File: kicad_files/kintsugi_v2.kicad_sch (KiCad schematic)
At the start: 162 parts, among them J1 Conn_01x04, J2 Conn_01x04, J3 AudioJack4, J4 AudioJack4, SW1 RotaryEncoder_Switch, SW2 SW_Push, U1 ProMicro, U2 MCP23017_SP

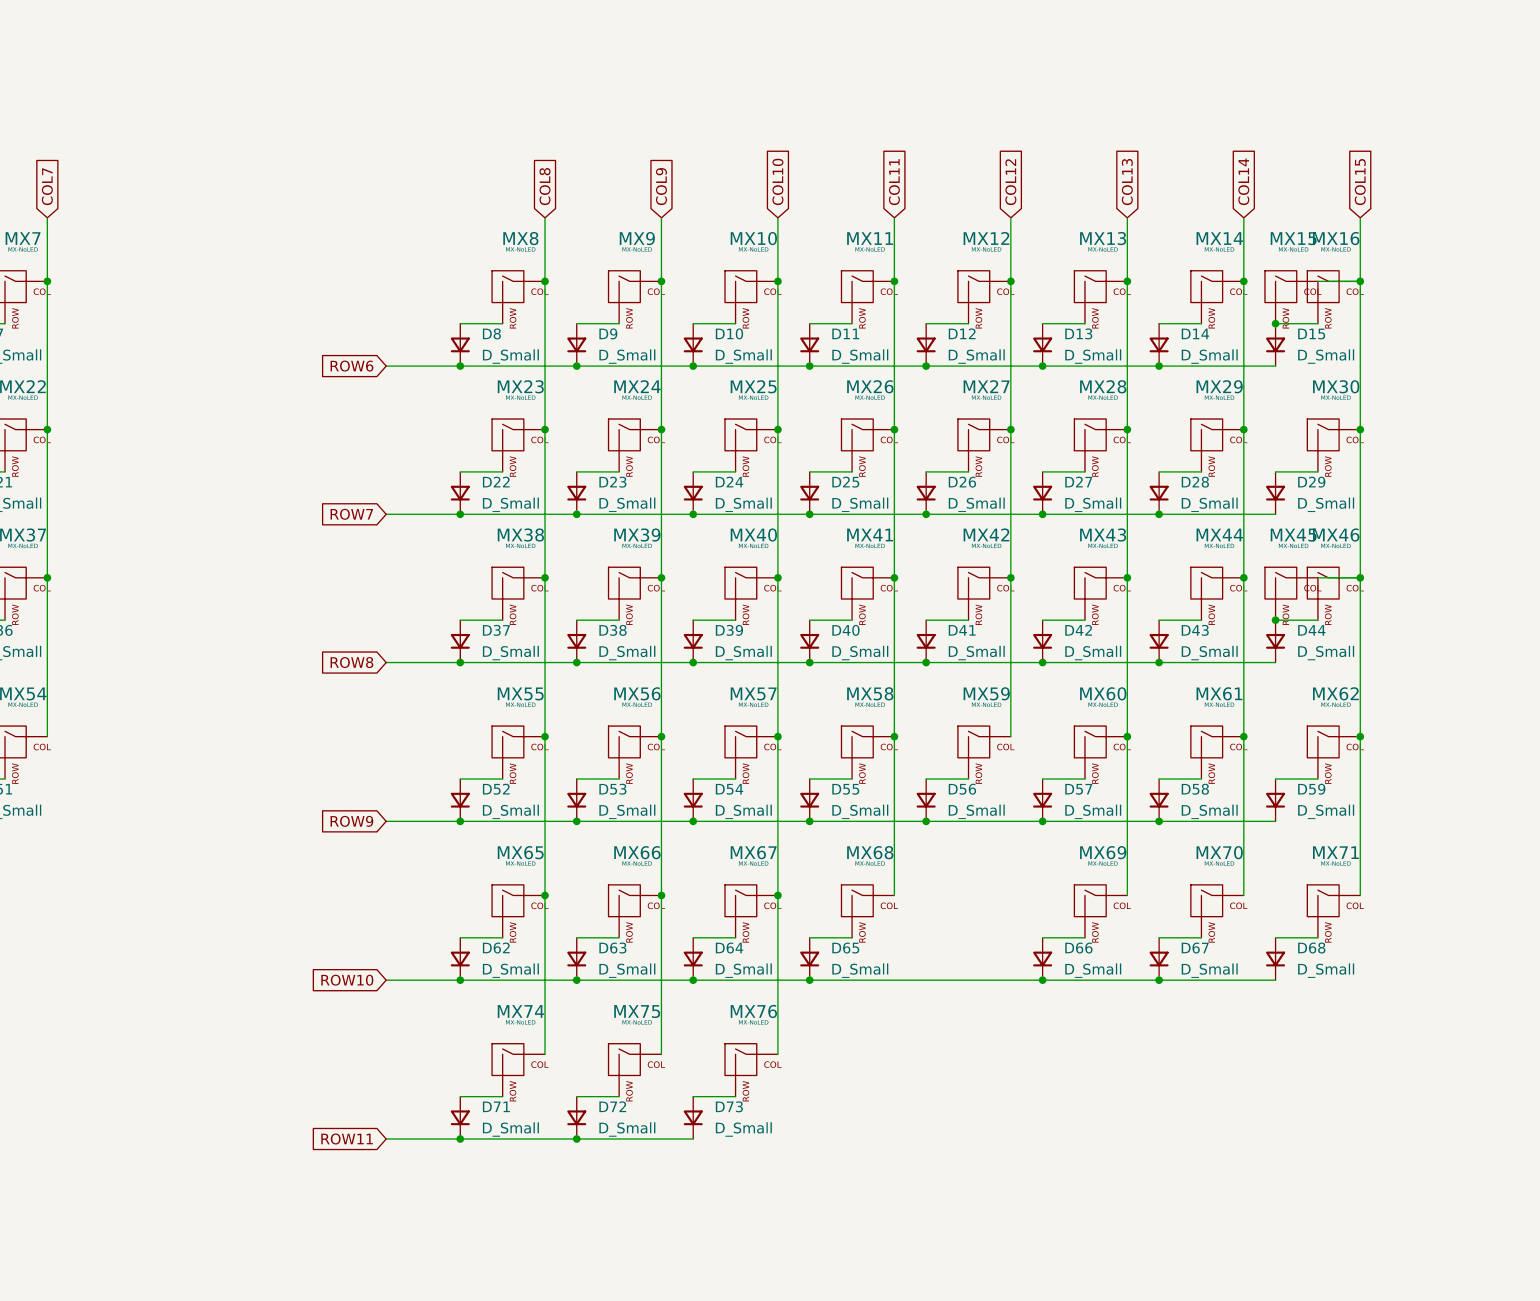
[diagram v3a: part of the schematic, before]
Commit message: Routed sockets pads to diodes. Pending review.
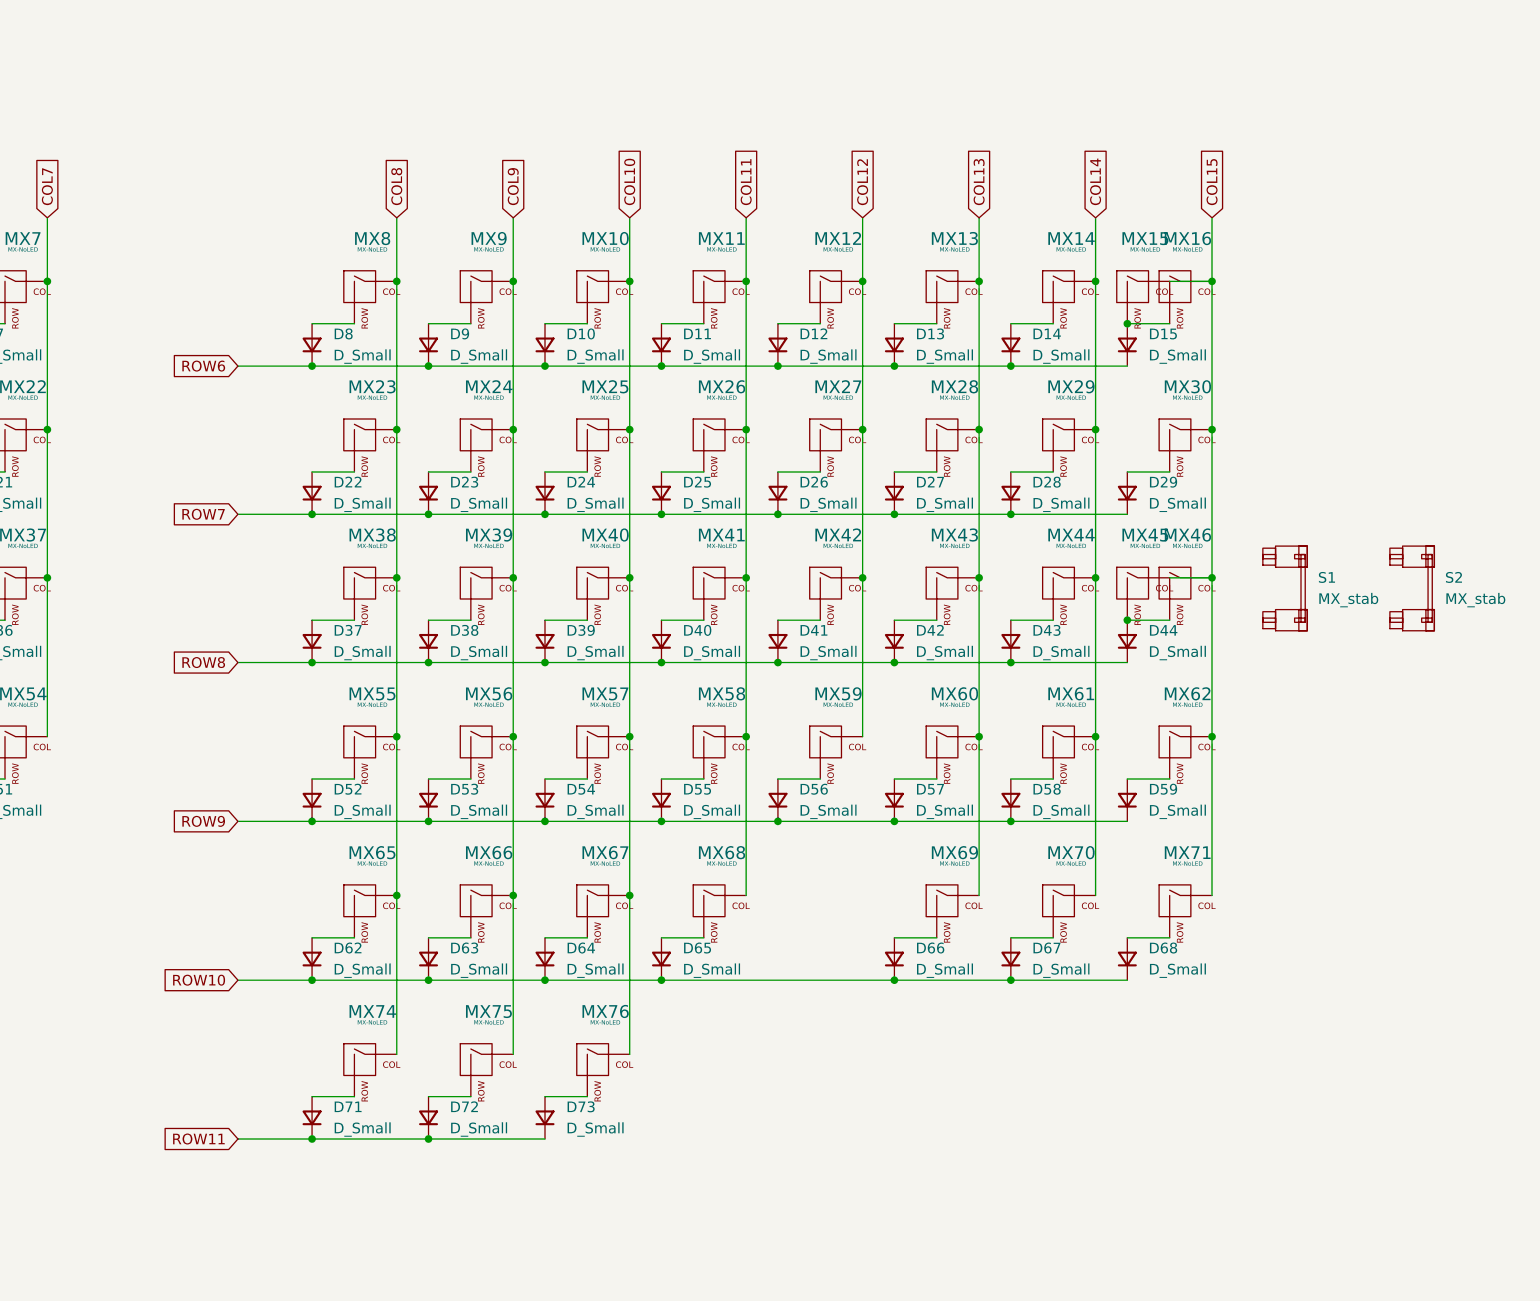
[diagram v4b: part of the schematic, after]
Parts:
- added S1: MX_stab, marbastlib-mx:STAB_MX_ISO_FLIPPED, symbol marbastlib-mx:MX_stab
- added S2: MX_stab, marbastlib-mx:STAB_MX_2.25u, symbol marbastlib-mx:MX_stab
- MX30: footprint acheron_MXH_metalrings:MX150H -> acheron_MXH_metalrings:MX100H
- MX45: footprint acheron_MXH_metalrings:MX225H -> acheron_MXH_metalrings:MX100H
- MX46: footprint acheron_MXH_metalrings:MX_ISOEnterH -> acheron_MXH_metalrings:MX100H
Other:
- moved on the sheet: D10, D11, D12, D13, D14, D15, D22, D23, D24, D25, D26, D27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

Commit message: Routed rows of the right side (down view) to the MCU.
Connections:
- net COL6: now also U1.13 (10/PB6); no longer U1.1 (TX0/PD3)
- net COL7: now also U1.14 (16/PB2); no longer U1.2 (RX1/PD2)
- net ENCA: now also U1.12 (9/PB5); no longer U1.11 (8/PB4)
- net ENCB: now also U1.11 (8/PB4); no longer U1.12 (9/PB5)
- net ROW0: now also U1.1 (TX0/PD3); no longer U1.7 (4/PD4)
- net ROW1: now also U1.2 (RX1/PD2); no longer U1.8 (5/PC6)
- net ROW2: now also U1.7 (4/PD4); no longer U1.9 (6/PD7)
- net ROW3: now also U1.8 (5/PC6); no longer U1.10 (7/PE6)
- net ROW4: now also U1.10 (7/PE6); no longer U1.13 (10/PB6)
- net ROW5: now also U1.9 (6/PD7); no longer U1.14 (16/PB2)

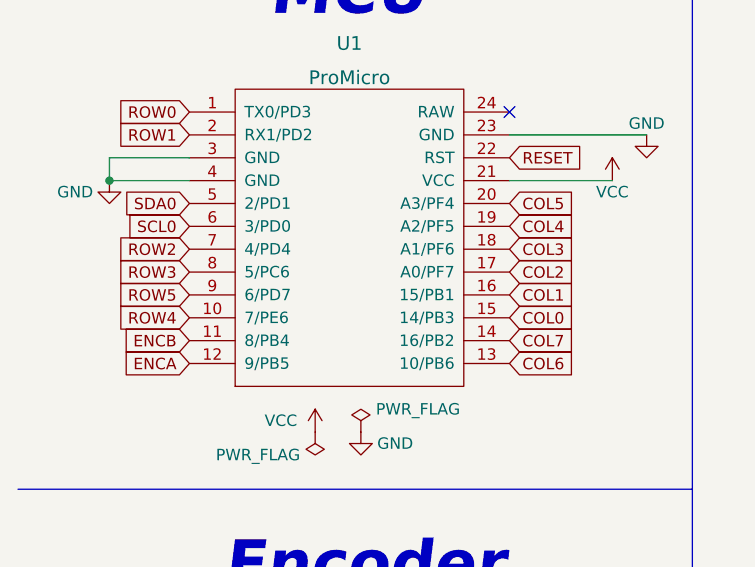
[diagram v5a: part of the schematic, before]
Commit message: Filleted edge cuts.
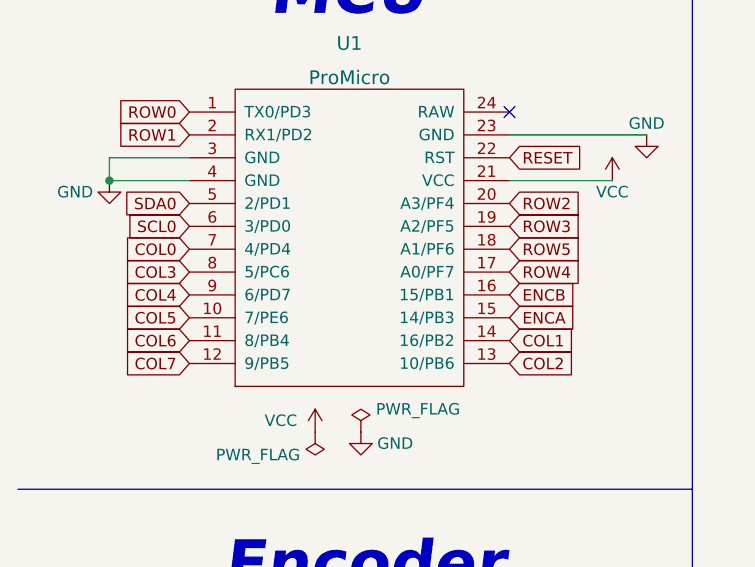
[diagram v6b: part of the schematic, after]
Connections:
- net COL0: now also U1.7 (4/PD4); no longer U1.15 (14/PB3)
- net COL1: now also U1.14 (16/PB2); no longer U1.16 (15/PB1)
- net COL2: now also U1.13 (10/PB6); no longer U1.17 (A0/PF7)
- net COL3: now also U1.8 (5/PC6); no longer U1.18 (A1/PF6)
- net COL4: now also U1.9 (6/PD7); no longer U1.19 (A2/PF5)
- net COL5: now also U1.10 (7/PE6); no longer U1.20 (A3/PF4)
- net COL6: now also U1.11 (8/PB4); no longer U1.13 (10/PB6)
- net COL7: now also U1.12 (9/PB5); no longer U1.14 (16/PB2)
- net ENCA: now also U1.15 (14/PB3); no longer U1.12 (9/PB5)
- net ENCB: now also U1.16 (15/PB1); no longer U1.11 (8/PB4)
- net ROW2: now also U1.20 (A3/PF4); no longer U1.7 (4/PD4)
- net ROW3: now also U1.19 (A2/PF5); no longer U1.8 (5/PC6)
- net ROW4: now also U1.17 (A0/PF7); no longer U1.10 (7/PE6)
- net ROW5: now also U1.18 (A1/PF6); no longer U1.9 (6/PD7)

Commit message: Added mousebites, re-arranged PCB and ground-filled half of the keyboard.
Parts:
- added H1, H10, H11, H12, H2, H3, H4, H5, H6, H7, H8, H9: MountingHole, Keebio-Parts:breakaway-mousebites, symbol Mechanical:MountingHole

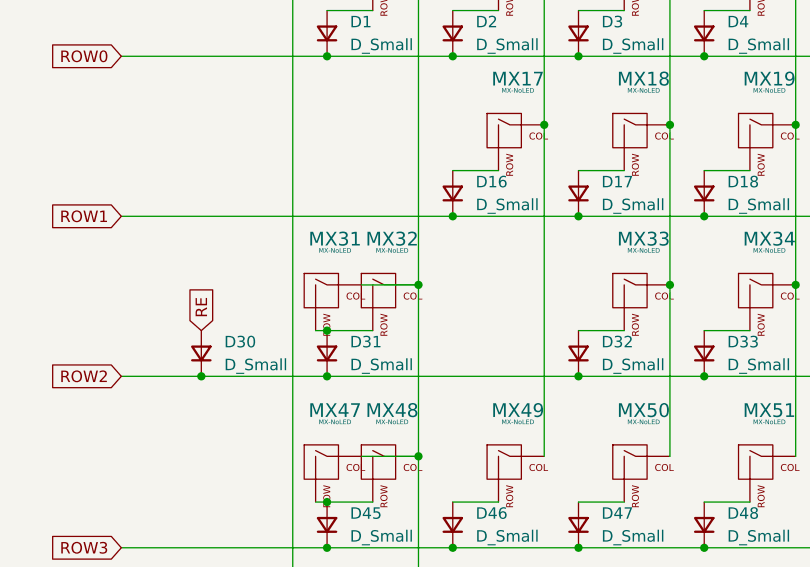
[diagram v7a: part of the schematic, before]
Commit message: Fixed some errors on the layout of the switch matrix.
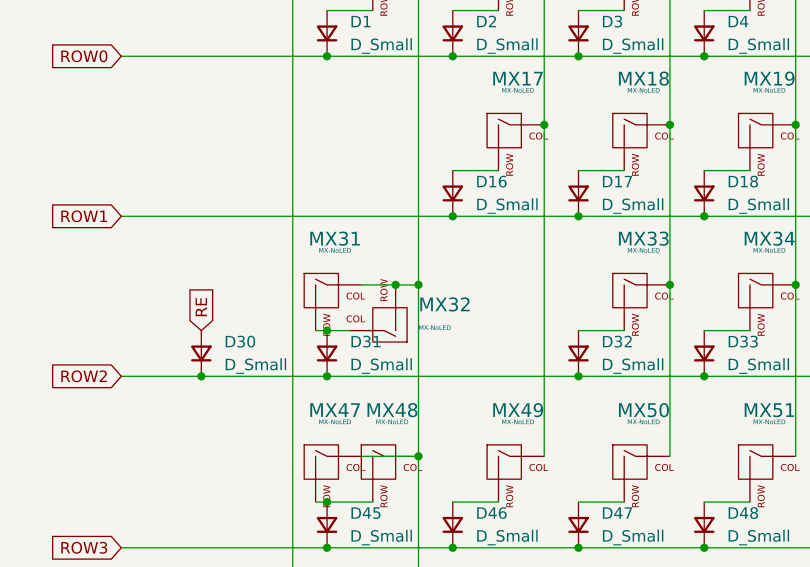
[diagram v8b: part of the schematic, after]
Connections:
- net COL1: now also MX32.2 (ROW); no longer MX32.1 (COL)
- net at D31.2 (A), MX31.2 (ROW): now also MX32.1 (COL); no longer MX32.2 (ROW)
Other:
- moved on the sheet: MX32
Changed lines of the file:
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@@
   (junction (at 149.86 72.39) (diameter 0) (color 0 0 0 0)
   )
+  (junction (at 135.89 85.09) (diameter 0) (color 0 0 0 0)
+  )
   (junction (at 275.59 54.61) (diameter 0) (color 0 0 0 0)
   )
@@
   (junction (at 285.75 80.01) (diameter 0) (color 0 0 0 0)
   )
-  (junction (at 135.89 85.09) (diameter 0) (color 0 0 0 0)
-  )
   (junction (at 299.72 80.01) (diameter 0) (color 0 0 0 0)
   )
@@
   (junction (at 215.9 44.45) (diameter 0) (color 0 0 0 0)
   )
+  (junction (at 143.51 80.01) (diameter 0) (color 0 0 0 0)
+  )
   (junction (at 299.72 99.06) (diameter 0) (color 0 0 0 0)
   )
@@
     (stroke (width 0) (type default) (color 0 0 0 0))
   )
+  (wire (pts (xy 143.51 80.01) (xy 146.05 80.01))
+    (stroke (width 0) (type default) (color 0 0 0 0))
+  )
   (wire (pts (xy 205.74 85.09) (xy 210.82 85.09))
     (stroke (width 0) (type default) (color 0 0 0 0))
@@
     (stroke (width 0) (type default) (color 0 0 0 0))
   )
+  (wire (pts (xy 139.7 80.01) (xy 143.51 80.01))
+    (stroke (width 0) (type default) (color 0 0 0 0))
+  )
   (polyline (pts (xy 87.63 115.57) (xy 87.63 77.47))
     (stroke (width 0) (type default) (color 0 0 0 0))
@@
     (stroke (width 0) (type default) (color 0 0 0 0))
   )
-  (wire (pts (xy 135.89 85.09) (xy 140.97 85.09))
-    (stroke (width 0) (type default) (color 0 0 0 0))
-  )
   (wire (pts (xy 205.74 67.31) (xy 210.82 67.31))
     (stroke (width 0) (type default) (color 0 0 0 0))
@@
     (stroke (width 0) (type default) (color 0 0 0 0))
   )
+  (wire (pts (xy 135.89 85.09) (xy 138.43 85.09))
+    (stroke (width 0) (type default) (color 0 0 0 0))
+  )
   (wire (pts (xy 299.72 62.23) (xy 299.72 80.01))
     (stroke (width 0) (type default) (color 0 0 0 0))
@@
     (stroke (width 0) (type default) (color 0 0 0 0))
   )
-  (wire (pts (xy 139.7 80.01) (xy 146.05 80.01))
-    (stroke (width 0) (type default) (color 0 0 0 0))
-  )
   (wire (pts (xy 163.83 54.61) (xy 177.8 54.61))
     (stroke (width 0) (type default) (color 0 0 0 0))
@@
     (pin "2")
   )
-  (symbol (lib_id "MX_Alps_Hybrid:MX-NoLED") (at 142.24 81.28 0) (unit 1)
+  (symbol (lib_id "MX_Alps_Hybrid:MX-NoLED") (at 142.24 83.82 180) (unit 1)
     (in_bom yes) (on_board yes) (fields_autoplaced)
-    (property "Reference" "MX32" (id 0) (at 143.1256 74.93 0)
-      (effects (font (size 1.524 1.524)))
+    (property "Reference" "MX32" (id 0) (at 146.05 82.2393 0)
+      (effects (font (size 1.524 1.524)) (justify right))
     )
-    (property "Value" "MX-NoLED" (id 1) (at 143.1256 76.2 0)
-      (effects (font (size 0.508 0.508)))
+    (property "Value" "MX-NoLED" (id 1) (at 146.05 84.7792 0)
+      (effects (font (size 0.508 0.508)) (justify right))
     )
-    (property "Footprint" "acheron_MXH_metalrings:MX175H" (id 2) (at 126.365 81.915 0)
+    (property "Footprint" "acheron_MXH_metalrings:MX175H" (id 2) (at 158.115 83.185 0)
       (effects (font (size 1.524 1.524)) hide)
     )
-    (property "Datasheet" "" (id 3) (at 126.365 81.915 0)
+    (property "Datasheet" "" (id 3) (at 158.115 83.185 0)
       (effects (font (size 1.524 1.524)) hide)
     )
